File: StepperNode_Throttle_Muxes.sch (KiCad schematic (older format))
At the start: 7 parts, among them P2 TE_640456-8, P3 TE_640456-8, U2 MAX4948ETG+, U3 MAX4948ETG+

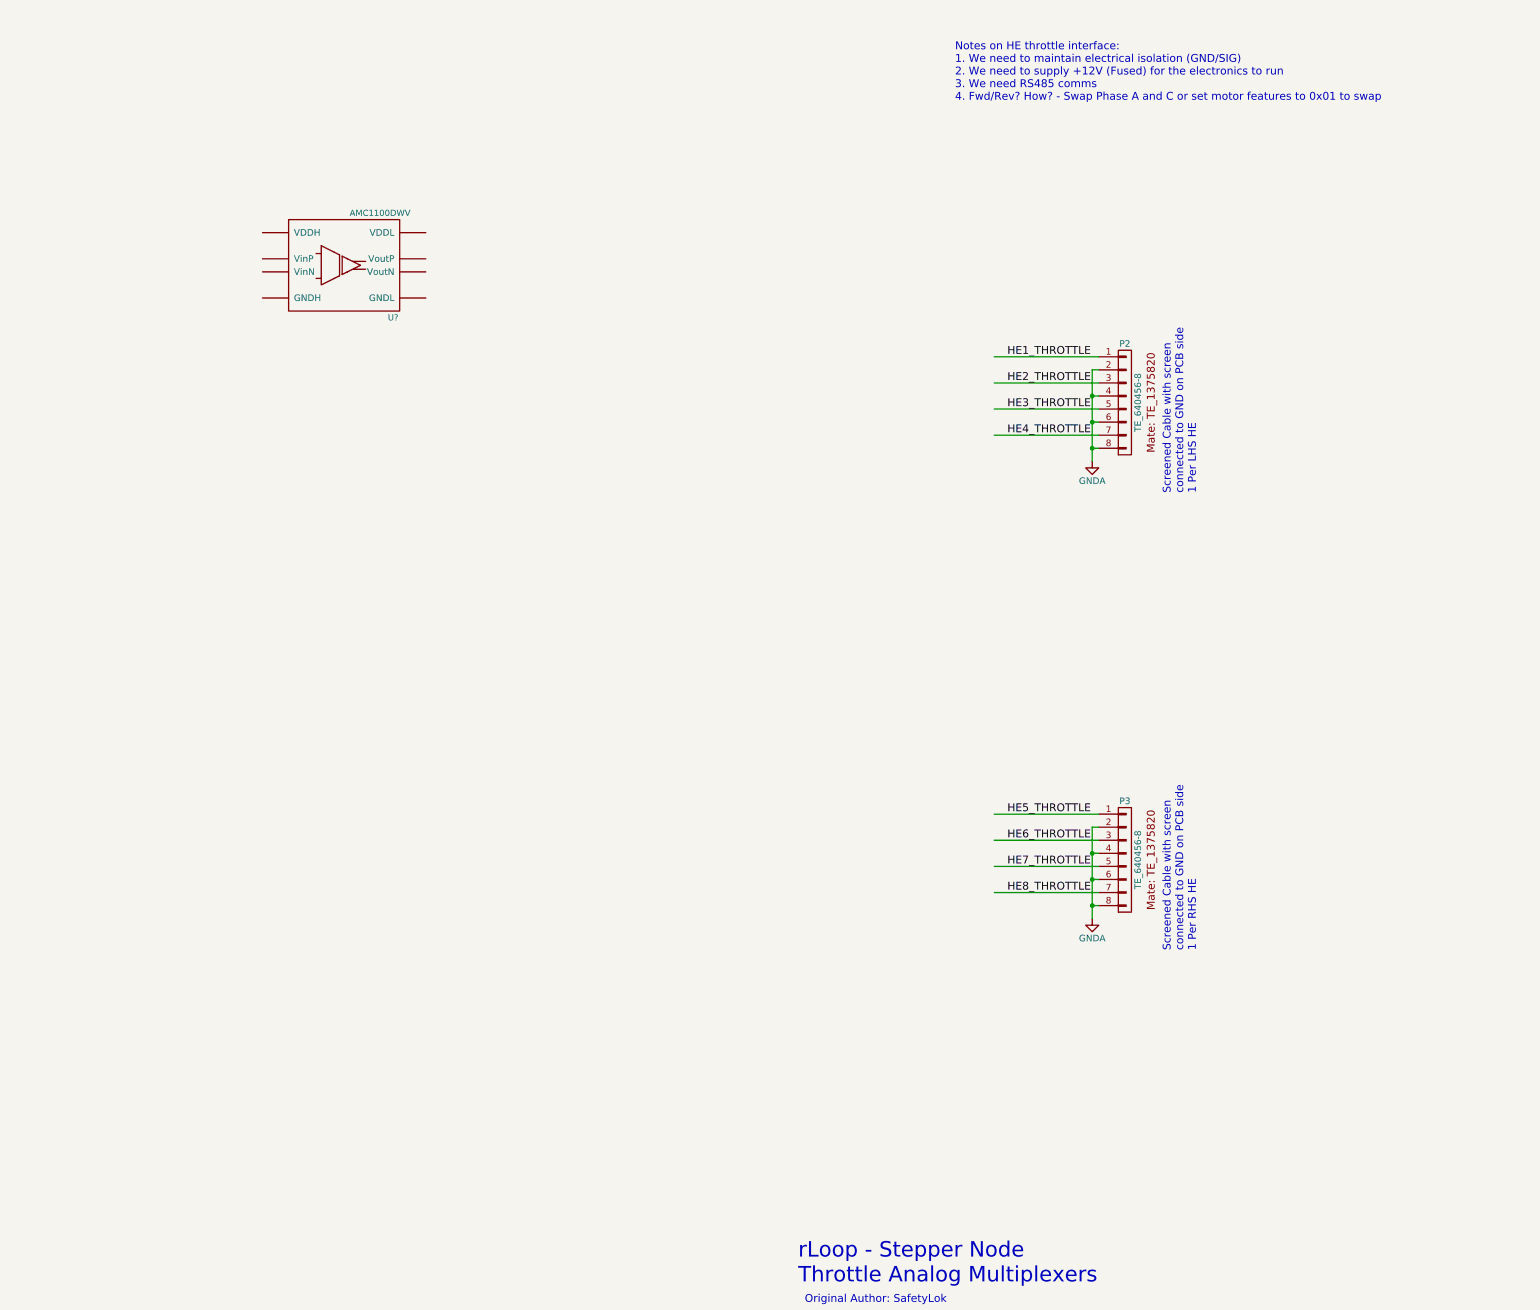
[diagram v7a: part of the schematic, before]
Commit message: Finish isolation and add brake limit switches.
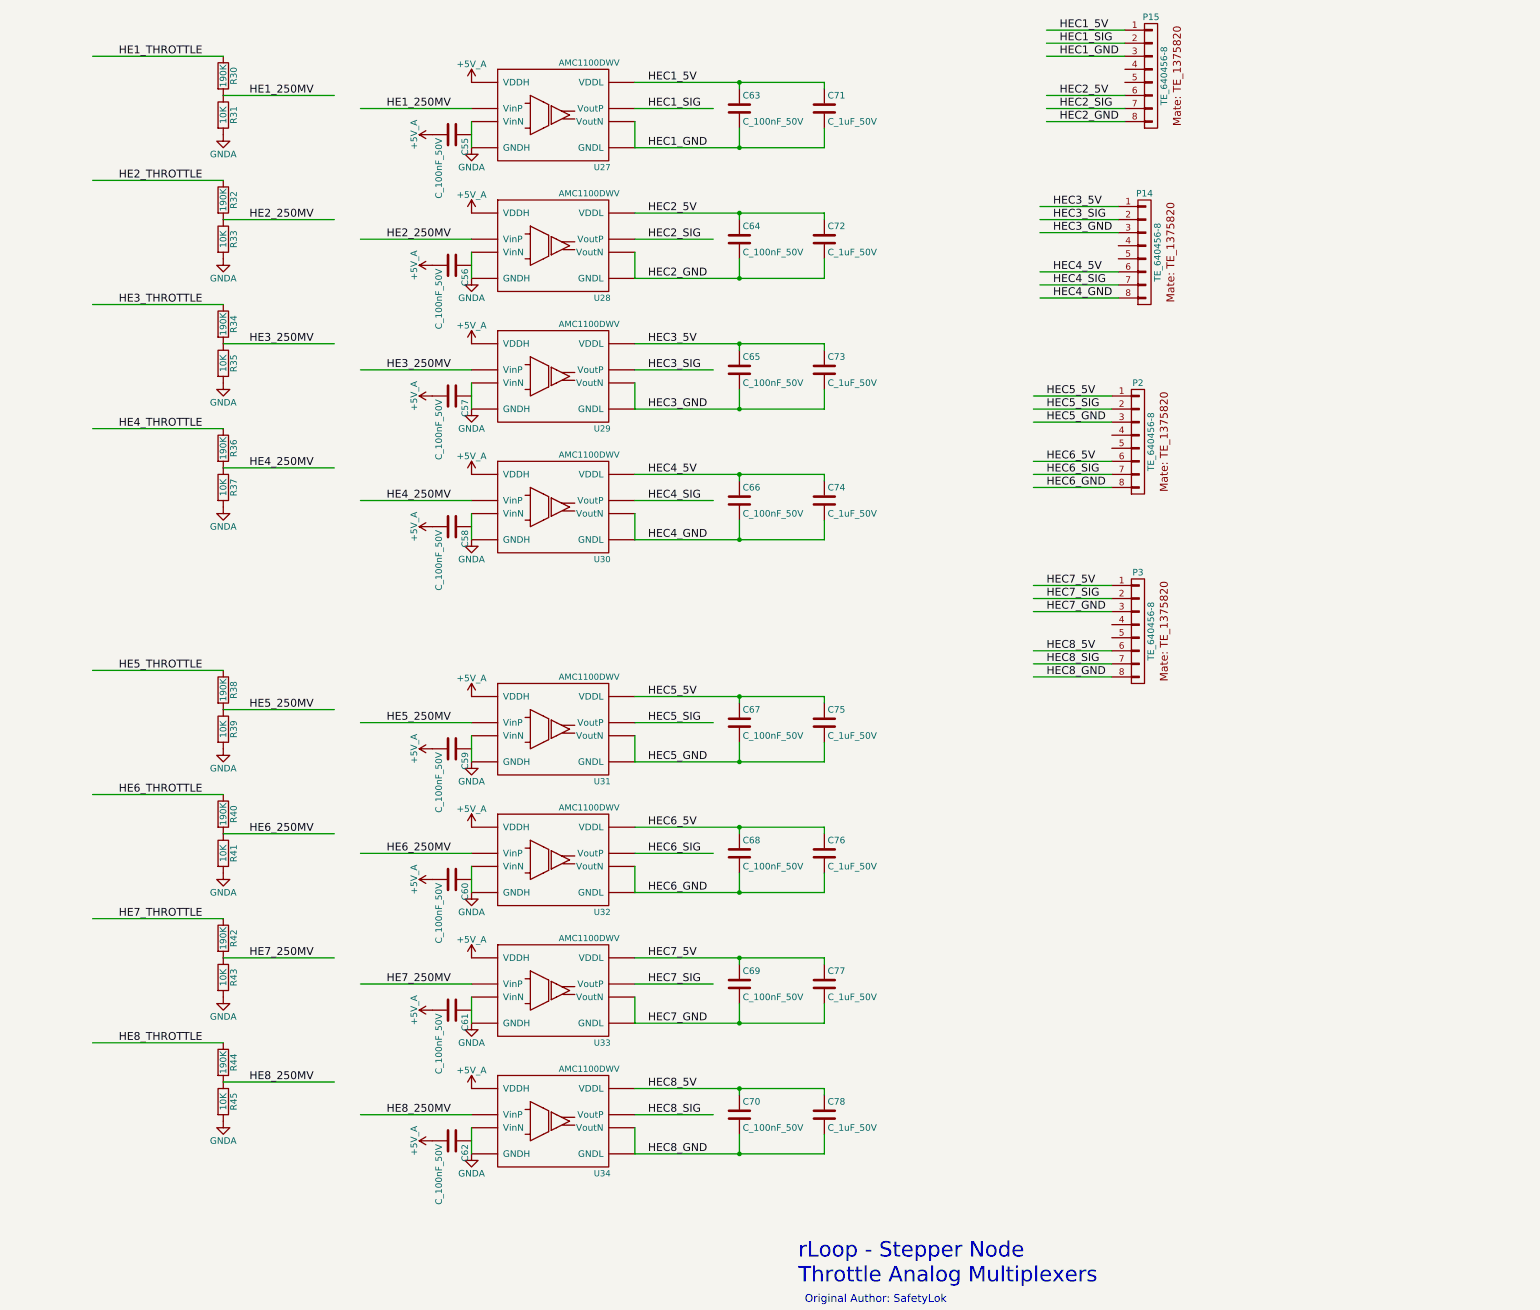
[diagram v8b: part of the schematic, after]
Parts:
- added C55, C56, C57, C58, C59, C60, C61, C62, C63, C64, C65, C66, C67, C68, C69, C70: C_100nF_50V, RLOOP_FOOTPRINTS:rLoop_C_0603, symbol C_100nF_50V
- added C71, C72, C73, C74, C75, C76, C77, C78: C_1uF_50V, RLOOP_FOOTPRINTS:rLoop_C_0603, symbol C_1uF_50V
- added P14, P15: TE_640456-8, RLOOP_FOOTPRINTS:rLoop_TE640456-8, symbol TE_640456-8
- added R30, R32, R34, R36, R38, R40, R42, R44: 190K, RLOOP_FOOTPRINTS:rLoop_R_0603, symbol 190K
- added R31, R33, R35, R37, R39, R41, R43, R45: 10K, RLOOP_FOOTPRINTS:rLoop_R_0603, symbol 10K
- added U28, U29, U30, U31, U32, U33, U34: AMC1100DWV, RLOOP_FOOTPRINTS:rLoop_SOIC8, symbol AMC1100DWV
- gave numbers to parts that had none: 1
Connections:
- net labels added: HE1_250MV, HE2_250MV, HE3_250MV, HE4_250MV, HE5_250MV, HE6_250MV, HE7_250MV, HE8_250MV, HEC1_5V, HEC1_GND, HEC1_SIG, HEC2_5V, HEC2_GND, HEC2_SIG, HEC3_5V, HEC3_GND, HEC3_SIG, HEC4_5V, HEC4_GND, HEC4_SIG, HEC5_5V, HEC5_GND, HEC5_SIG, HEC6_5V, HEC6_GND, HEC6_SIG, HEC7_5V, HEC7_GND, HEC7_SIG, HEC8_5V, HEC8_GND, HEC8_SIG
- wire segments 64 -> 166
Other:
- note removed: "Notes on HE throttle interface:\n1. We need to maintain electrical isolation (GND/SIG)\n2. We need to supply +12V (Fused) for the electronics to run\n3. We need RS485 comms\n4. Fwd/Rev? How? - Swap Phase A and C or set motor features to 0x01 to swap\n"
- note removed: "Screened Cable with screen\nconnected to GND on PCB side\n1 Per LHS HE"
- note removed: "Screened Cable with screen\nconnected to GND on PCB side\n1 Per RHS HE"
- moved on the sheet: U27
